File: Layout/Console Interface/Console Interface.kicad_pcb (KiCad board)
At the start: 2 copper layers, 63.9 x 20.5 mm, 58 parts, among them J1 USB_C_Receptacle_USB2.0, J2 Conn_01x04_Socket, J3 Conn_01x04_Socket, J4 Conn_01x04_Socket, J6 Conn_01x04_Socket, Q1 AO3401A, SW1 SW_BOOT, SW3 SW_PAIR, U1 W25Q32JVSS, U2 RP2040, U4 MIC5504-3.3YM5, U5 MIC5504-3.3YM5, Y1 Crystal_GND24

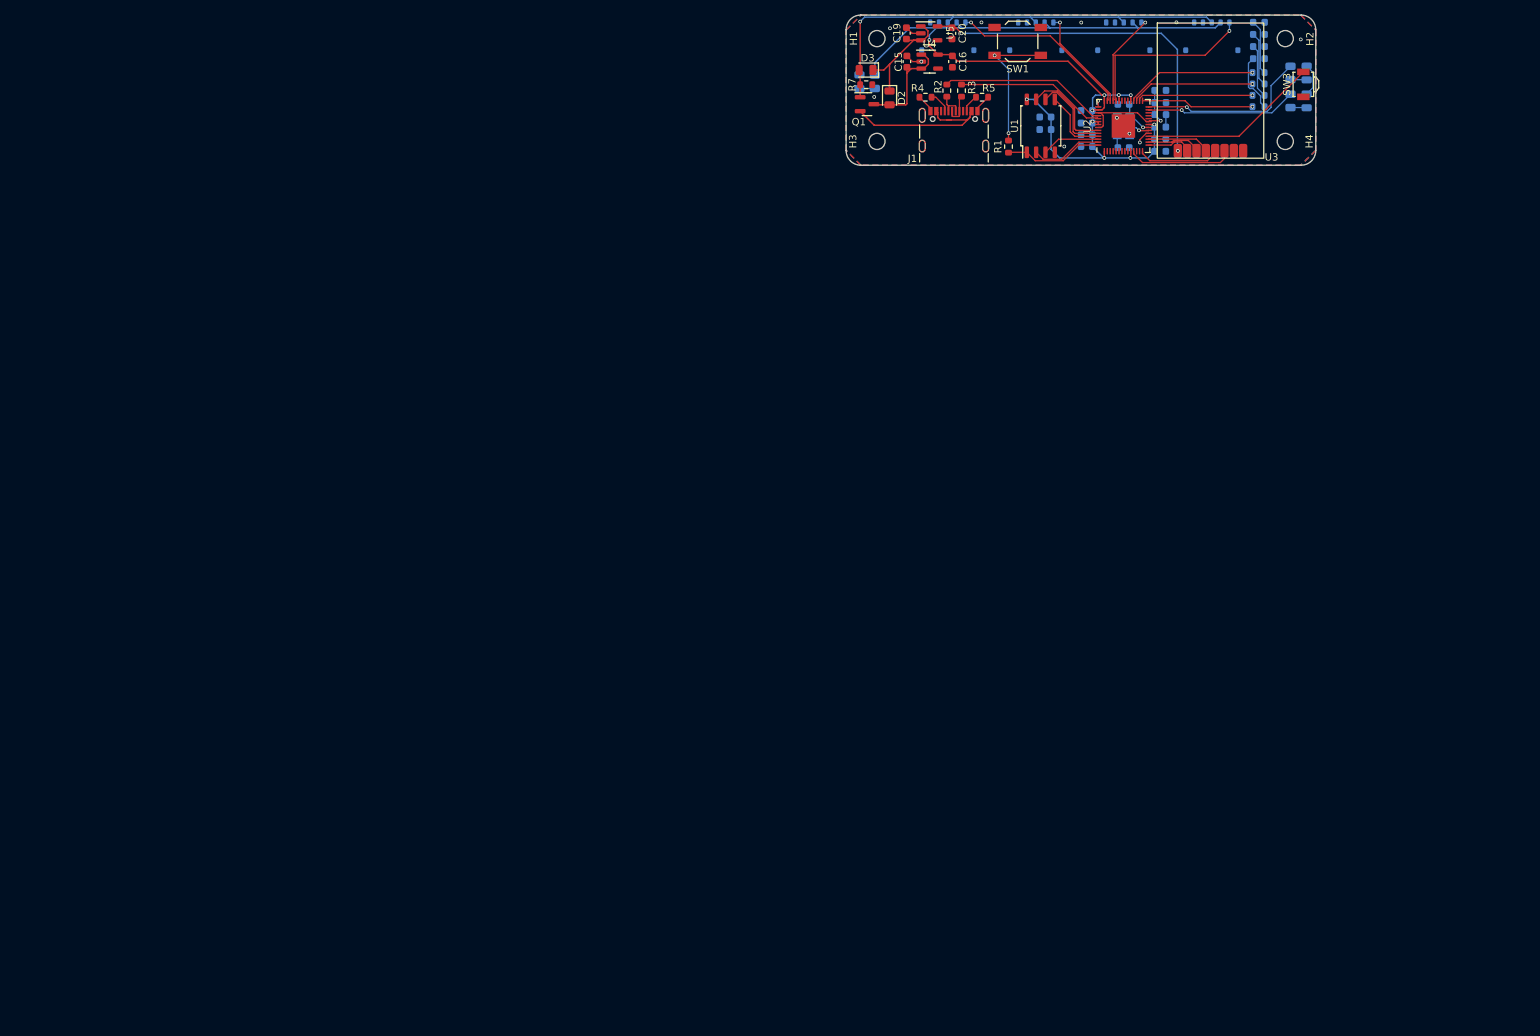
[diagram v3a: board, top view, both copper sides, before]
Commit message: Use separate board for lights
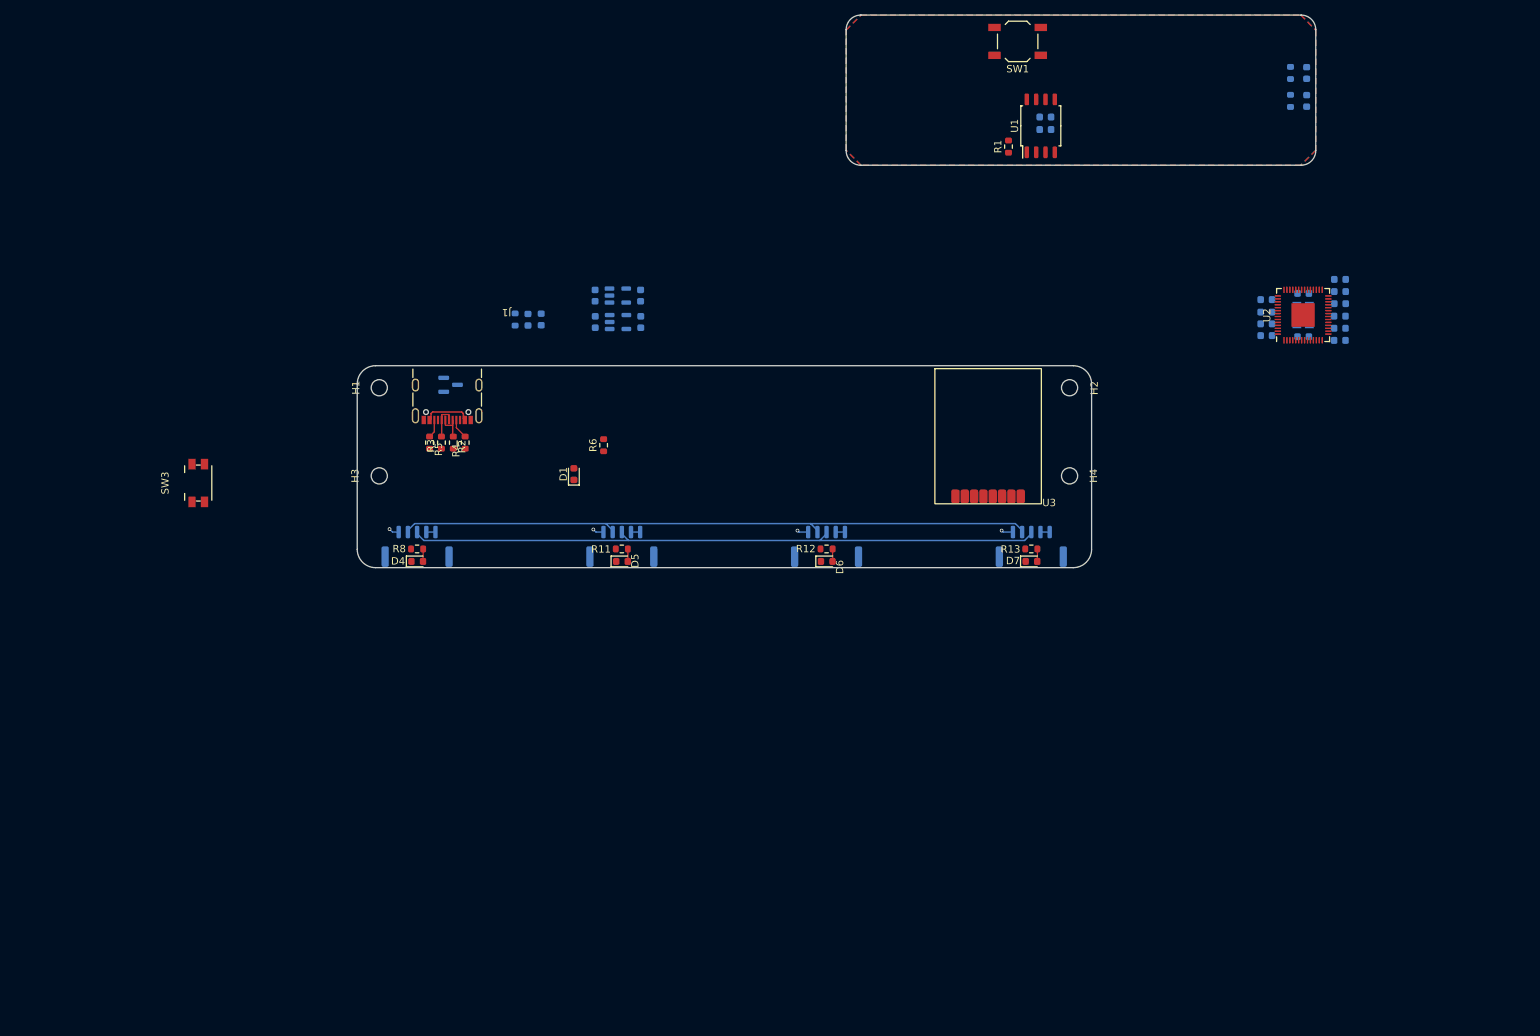
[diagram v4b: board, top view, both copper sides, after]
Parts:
- C15, C16, C19, C20, Q1, R7, U4, U5: moved to B.Cu
- D1: footprint LED_SMD:LED_0805_2012Metric -> LED_SMD:LED_0603_1608Metric; moved to F.Cu
- D2, D3: footprint Diode_SMD:D_0805_2012Metric -> Diode_SMD:D_0603_1608Metric; moved to B.Cu
- D4, D5, D6, D7, R11, R12, R13, R8: moved to F.Cu
- D8, D9: footprint LED_SMD:LED_0805_2012Metric -> LED_SMD:LED_0603_1608Metric
- J2, J3, J4, J6: footprint Connector_Molex:Molex_Pico-EZmate_78171-0005_1x05-1MP_P1.20mm_Vertical -> Connector_JST:JST_GH_BM05B-GHS-TBT_1x05-1MP_P1.25mm_Vertical
- R16, R17: footprint Resistor_SMD:R_0805_2012Metric -> Resistor_SMD:R_0603_1608Metric
- R6: footprint Resistor_SMD:R_0805_2012Metric -> Resistor_SMD:R_0603_1608Metric; moved to F.Cu
- SW3: footprint Button_Switch_SMD:SW_SPST_B3U-3000P -> Button_Switch_SMD:Panasonic_EVQPUK_EVQPUB
- moved SW3 160.0 mm to (66.0, 97.0), turned to 90 degrees
- moved D4 136.1 mm to (95.8, 107.7), turned to 0 degrees
- moved R8 131.7 mm to (95.8, 106.0)
- moved D5 112.6 mm to (123.7, 107.7), turned to 0 degrees
- moved R11 107.4 mm to (123.6, 106.0)
- moved J6 100.2 mm to (95.8, 105.6), turned to 0 degrees
- moved D6 91.5 mm to (151.5, 107.7), turned to 0 degrees
- moved J2 89.5 mm to (123.6, 105.6), turned to 0 degrees
- moved R5 88.7 mm to (97.5, 91.5), turned to -90 degrees
- moved R3 85.5 mm to (99.1, 91.5), turned to -90 degrees
- moved R12 85.3 mm to (151.5, 106.0)
- moved H1 82.8 mm to (90.6, 84.0)
- moved R2 82.5 mm to (100.7, 91.5), turned to -90 degrees
- moved H3 81.7 mm to (90.6, 96.0)
- moved J3 80.4 mm to (151.5, 105.6), turned to 0 degrees
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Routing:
- net +3.3V: track 47.8 -> 0.00 mm, vias 2 -> 0
- net +3.3V_A: track 135.5 -> 87.9 mm, vias 10 -> 0
- net +5V: track 61.9 -> 88.0 mm, vias 1 -> 0
- net /Processor/PAIR: track 24.7 -> 0.00 mm
- net TX_LED: track 23.9 -> 0.00 mm, vias 1 -> 0
- net DATA_1: track 24.4 -> 1.42 mm
- net /Processor/USB_DM: track 22.8 -> 0.00 mm
- net DATA_4: track 24.3 -> 1.62 mm
- net /Processor/USB_DP: track 20.5 -> 0.00 mm
- net RX_LED: track 20.5 -> 0.00 mm, vias 1 -> 0
- net Net-(R1-Pad2): track 18.7 -> 0.00 mm, vias 2 -> 0
- net CONT_1: track 18.0 -> 0.00 mm, vias 1 -> 0
- net Net-(D2-K): track 17.6 -> 0.26 mm
- net CONT_2: track 16.9 -> 0.00 mm, vias 1 -> 0
- net VBUS: track 23.4 -> 6.76 mm
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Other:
- board size 63.9 x 20.5 mm -> 130.5 x 75.2 mm
